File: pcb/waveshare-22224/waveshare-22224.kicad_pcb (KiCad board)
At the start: 2 copper layers, 20.6 x 8.2 mm, 4 parts, among them J2 Conn_01x08_Socket

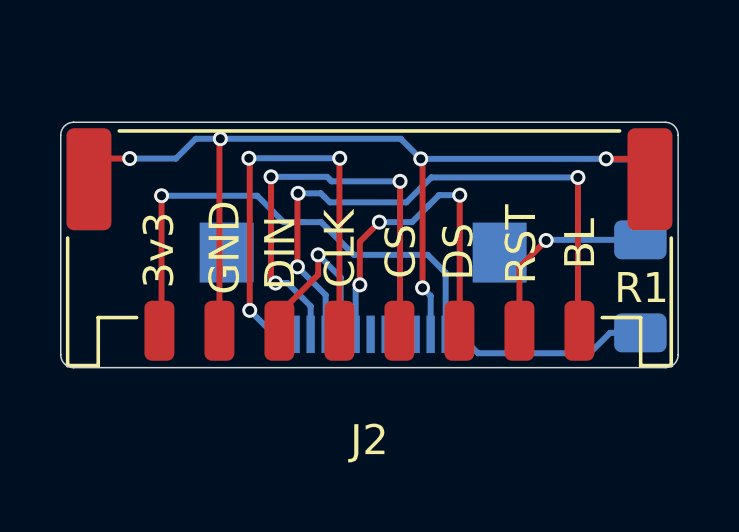
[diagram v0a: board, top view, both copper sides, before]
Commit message: made waveshare 22224 pcb large enough for jlcpcb PCBA
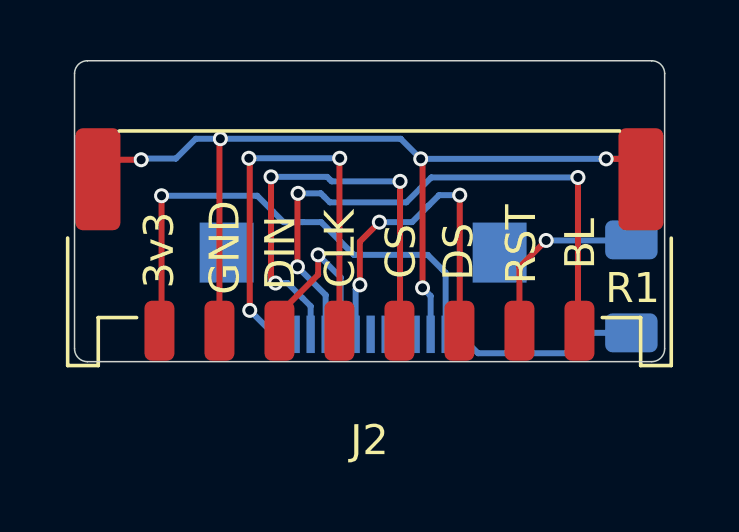
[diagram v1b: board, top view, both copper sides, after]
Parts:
- moved R1 0.30 mm to (184.3, 106.6)
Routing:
- net GND: track 33.4 -> 32.8 mm
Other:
- board size 20.6 x 8.2 mm -> 19.7 x 10 mm
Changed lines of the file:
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@@
     (pad "8" smd roundrect (at 7 -2.9 180) (size 1 2) (layers "F.Cu" "F.Paste" "F.Mask") (roundrect_rratio 0.25)
       (net 7 "+3V3") (pinfunction "Pin_8") (pintype "passive"))
-    (pad "9" smd roundrect (at -9.35 2.15 180) (size 1.5 3.4) (layers "F.Cu" "F.Paste" "F.Mask") (roundrect_rratio 0.1666673333)
+    (pad "9" smd roundrect (at -9.05 2.15 180) (size 1.5 3.4) (layers "F.Cu" "F.Paste" "F.Mask") (roundrect_rratio 0.1666673333)
       (net 1 "GND") (pinfunction "GND") (pintype "passive"))
-    (pad "9" smd roundrect (at 9.35 2.15 180) (size 1.5 3.4) (layers "F.Cu" "F.Paste" "F.Mask") (roundrect_rratio 0.1666673333)
+    (pad "9" smd roundrect (at 9.05 2.15 180) (size 1.5 3.4) (layers "F.Cu" "F.Paste" "F.Mask") (roundrect_rratio 0.1666673333)
       (net 1 "GND") (pinfunction "GND") (pintype "passive"))
     (model "${KICAD6_3DMODEL_DIR}/Connector_JST.3dshapes/JST_PH_S8B-PH-SM4-TB_1x08-1MP_P2.00mm_Horizontal.wrl"
@@
   )
   (footprint "Resistor_SMD:R_1206_3216Metric_Pad1.30x1.75mm_HandSolder" (layer "B.Cu")
-    (at 184.6 106.58 -90)
+    (at 184.3 106.58 -90)
     (descr "Resistor SMD 1206 (3216 Metric), square (rectangular) end terminal, IPC_7351 nominal with elongated pad for handsoldering. (Body size source: IPC-SM-782 page 72, https://www.pcb-3d.com/wordpress/wp-content/uploads/ipc-sm-782a_amendment_1_and_2.pdf), generated with kicad-footprint-generator")
     (tags "resistor handsolder")
@@
     (pad "14" smd rect (at -4.55 -0.686) (size 1.8 2) (layers "B.Cu" "B.Paste" "B.Mask"))
   )
-  (gr_line (start 165.71 109.29) (end 185.43 109.29)
-    (stroke (width 0.05) (type default)) (layer "Edge.Cuts"))
-  (gr_arc (start 165.71 109.29) (mid 165.405944 109.164056) (end 165.28 108.86)
-    (stroke (width 0.05) (type default)) (layer "Edge.Cuts"))
-  (gr_arc (start 185.86 108.86) (mid 185.734056 109.164056) (end 185.43 109.29)
-    (stroke (width 0.05) (type default)) (layer "Edge.Cuts"))
-  (gr_line (start 165.28 101.54) (end 165.28 108.86)
-    (stroke (width 0.05) (type default)) (layer "Edge.Cuts"))
-  (gr_line (start 165.71 101.11) (end 185.43 101.11)
-    (stroke (width 0.05) (type default)) (layer "Edge.Cuts"))
-  (gr_arc (start 185.43 101.11) (mid 185.734056 101.235944) (end 185.86 101.54)
-    (stroke (width 0.05) (type default)) (layer "Edge.Cuts"))
-  (gr_arc (start 165.28 101.54) (mid 165.405944 101.235944) (end 165.71 101.11)
-    (stroke (width 0.05) (type default)) (layer "Edge.Cuts"))
-  (gr_line (start 185.86 101.54) (end 185.86 108.86)
+  (gr_line (start 166.17 109.09) (end 184.98 109.09)
+    (stroke (width 0.05) (type default)) (layer "Edge.Cuts"))
+  (gr_arc (start 166.17 109.09) (mid 165.865944 108.964056) (end 165.74 108.66)
+    (stroke (width 0.05) (type default)) (layer "Edge.Cuts"))
+  (gr_arc (start 185.41 108.66) (mid 185.284056 108.964056) (end 184.98 109.09)
+    (stroke (width 0.05) (type default)) (layer "Edge.Cuts"))
+  (gr_line (start 165.74 99.49) (end 165.74 108.66)
+    (stroke (width 0.05) (type default)) (layer "Edge.Cuts"))
+  (gr_line (start 166.17 99.06) (end 184.98 99.06)
+    (stroke (width 0.05) (type default)) (layer "Edge.Cuts"))
+  (gr_arc (start 184.98 99.06) (mid 185.284056 99.185944) (end 185.41 99.49)
+    (stroke (width 0.05) (type default)) (layer "Edge.Cuts"))
+  (gr_arc (start 165.74 99.49) (mid 165.865944 99.185944) (end 166.17 99.06)
+    (stroke (width 0.05) (type default)) (layer "Edge.Cuts"))
+  (gr_line (start 185.41 99.49) (end 185.41 108.66)
     (stroke (width 0.05) (type default)) (layer "Edge.Cuts"))
   (gr_text "BL" (at 183.18 106.01 90) (layer "F.SilkS")
@@
   (segment (start 170.57 101.69) (end 170.6 101.66) (width 0.2) (layer "F.Cu") (net 1))
   (segment (start 177.34 102.39) (end 177.28 102.33) (width 0.2) (layer "F.Cu") (net 1))
-  (segment (start 183.46 102.33) (end 184.24 102.33) (width 0.2) (layer "F.Cu") (net 1))
-  (segment (start 167.58 102.32) (end 166.91 102.32) (width 0.2) (layer "F.Cu") (net 1))
+  (segment (start 183.46 102.33) (end 183.94 102.33) (width 0.2) (layer "F.Cu") (net 1))
   (segment (start 177.34 106.63) (end 177.34 102.39) (width 0.2) (layer "F.Cu") (net 1))
   (segment (start 170.57 108.06) (end 170.57 101.69) (width 0.2) (layer "F.Cu") (net 1))
-  (segment (start 184.24 102.33) (end 184.92 103.01) (width 0.2) (layer "F.Cu") (net 1))
-  (segment (start 166.91 102.32) (end 166.22 103.01) (width 0.2) (layer "F.Cu") (net 1))
-  (via (at 167.58 102.32) (size 0.5) (drill 0.3) (layers "F.Cu" "B.Cu") (net 1))
+  (segment (start 167.96 102.36) (end 167.17 102.36) (width 0.2) (layer "F.Cu") (net 1))
+  (segment (start 167.17 102.36) (end 166.52 103.01) (width 0.2) (layer "F.Cu") (net 1))
+  (segment (start 183.94 102.33) (end 184.62 103.01) (width 0.2) (layer "F.Cu") (net 1))
+  (via (at 167.96 102.36) (size 0.5) (drill 0.3) (layers "F.Cu" "B.Cu") (net 1))
   (via (at 170.6 101.66) (size 0.5) (drill 0.3) (layers "F.Cu" "B.Cu") (net 1))
   (via (at 183.46 102.33) (size 0.5) (drill 0.3) (layers "F.Cu" "B.Cu") (net 1))
   (via (at 177.28 102.33) (size 0.5) (drill 0.3) (layers "F.Cu" "B.Cu") (net 1))
   (via (at 177.34 106.63) (size 0.5) (drill 0.3) (layers "F.Cu" "B.Cu") (net 1))
+  (segment (start 183.46 102.33) (end 184.62 102.33) (width 0.2) (layer "B.Cu") (net 1))
   (segment (start 169.12 102.32) (end 169.78 101.66) (width 0.2) (layer "B.Cu") (net 1))
+  (segment (start 184.62 102.33) (end 184.64 102.35) (width 0.2) (layer "B.Cu") (net 1))
+  (segment (start 169.12 102.32) (end 168 102.32) (width 0.2) (layer "B.Cu") (net 1))
   (segment (start 170.6 101.66) (end 176.61 101.66) (width 0.2) (layer "B.Cu") (net 1))
   (segment (start 183.46 102.33) (end 177.28 102.33) (width 0.2) (layer "B.Cu") (net 1))
   (segment (start 177.61 108.178) (end 177.61 106.9) (width 0.2) (layer "B.Cu") (net 1))
-  (segment (start 183.48 102.35) (end 183.46 102.33) (width 0.2) (layer "B.Cu") (net 1))
-  (segment (start 167.58 102.32) (end 169.12 102.32) (width 0.2) (layer "B.Cu") (net 1))
+  (segment (start 168 102.32) (end 167.96 102.36) (width 0.2) (layer "B.Cu") (net 1))
   (segment (start 169.78 101.66) (end 170.6 101.66) (width 0.2) (layer "B.Cu") (net 1))
   (segment (start 176.61 101.66) (end 177.28 102.33) (width 0.2) (layer "B.Cu") (net 1))
-  (segment (start 184.64 102.35) (end 183.48 102.35) (width 0.2) (layer "B.Cu") (net 1))
   (segment (start 177.61 106.9) (end 177.34 106.63) (width 0.2) (layer "B.Cu") (net 1))
   (segment (start 182.52 108.01) (end 182.57 108.06) (width 0.2) (layer "F.Cu") (net 4))
@@
   (via (at 168.64 103.56) (size 0.5) (drill 0.3) (layers "F.Cu" "B.Cu") (net 7))
   (segment (start 172.71 104.44) (end 172.35 104.08) (width 0.2) (layer "B.Cu") (net 7))
+  (segment (start 178.11 108.178) (end 178.558 108.178) (width 0.2) (layer "B.Cu") (net 7))
+  (segment (start 182.86 108.13) (end 184.3 108.13) (width 0.2) (layer "B.Cu") (net 7))
+  (segment (start 179.19 108.81) (end 182.18 108.81) (width 0.2) (layer "B.Cu") (net 7))
   (segment (start 177.51 105.53) (end 175.05 105.53) (width 0.2) (layer "B.Cu") (net 7))
   (segment (start 173.35 104.44) (end 172.71 104.44) (width 0.2) (layer "B.Cu") (net 7))
+  (segment (start 178.558 108.178) (end 179.19 108.81) (width 0.2) (layer "B.Cu") (net 7))
   (segment (start 178.11 108.178) (end 178.11 106.13) (width 0.2) (layer "B.Cu") (net 7))
   (segment (start 172.35 104.08) (end 171.83 103.56) (width 0.2) (layer "B.Cu") (net 7))
   (segment (start 178.11 106.13) (end 178 106.02) (width 0.2) (layer "B.Cu") (net 7))
-  (segment (start 178.558 108.178) (end 179.19 108.81) (width 0.2) (layer "B.Cu") (net 7))
   (segment (start 178 106.02) (end 177.51 105.53) (width 0.2) (layer "B.Cu") (net 7))
-  (segment (start 178.11 108.178) (end 178.558 108.178) (width 0.2) (layer "B.Cu") (net 7))
-  (segment (start 183.59 108.13) (end 184.6 108.13) (width 0.2) (layer "B.Cu") (net 7))
+  (segment (start 182.18 108.81) (end 182.86 108.13) (width 0.2) (layer "B.Cu") (net 7))
   (segment (start 175.05 105.53) (end 174.56 105.04) (width 0.2) (layer "B.Cu") (net 7))
-  (segment (start 182.91 108.81) (end 183.59 108.13) (width 0.2) (layer "B.Cu") (net 7))
-  (segment (start 179.19 108.81) (end 182.91 108.81) (width 0.2) (layer "B.Cu") (net 7))
   (segment (start 174.56 105.04) (end 173.96 104.44) (width 0.2) (layer "B.Cu") (net 7))
   (segment (start 171.83 103.56) (end 168.64 103.56) (width 0.2) (layer "B.Cu") (net 7))
@@
   (via (at 181.46 105.05) (size 0.5) (drill 0.3) (layers "F.Cu" "B.Cu") (net 13))
   (segment (start 184.6 103.35) (end 184.64 103.31) (width 0.2) (layer "B.Cu") (net 13))
+  (segment (start 181.46 105.05) (end 184.28 105.05) (width 0.2) (layer "B.Cu") (net 13))
+  (segment (start 184.28 105.05) (end 184.3 105.03) (width 0.2) (layer "B.Cu") (net 13))
   (segment (start 184.6 105.03) (end 184.6 103.35) (width 0.2) (layer "B.Cu") (net 13))
-  (segment (start 181.48 105.03) (end 181.46 105.05) (width 0.2) (layer "B.Cu") (net 13))
-  (segment (start 184.6 105.03) (end 181.48 105.03) (width 0.2) (layer "B.Cu") (net 13))
 )
